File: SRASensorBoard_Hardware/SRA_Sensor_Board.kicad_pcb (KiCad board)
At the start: 2 copper layers, 70 parts, among them J1 USB_B_Micro, Q1 CSD17305Q5A, U1 LM3478MMX_NOPB, U2 OKI, U3 OKI, U4 TM4C129E_Launchpad, U5 MAX232, U6 IRF7821PbF

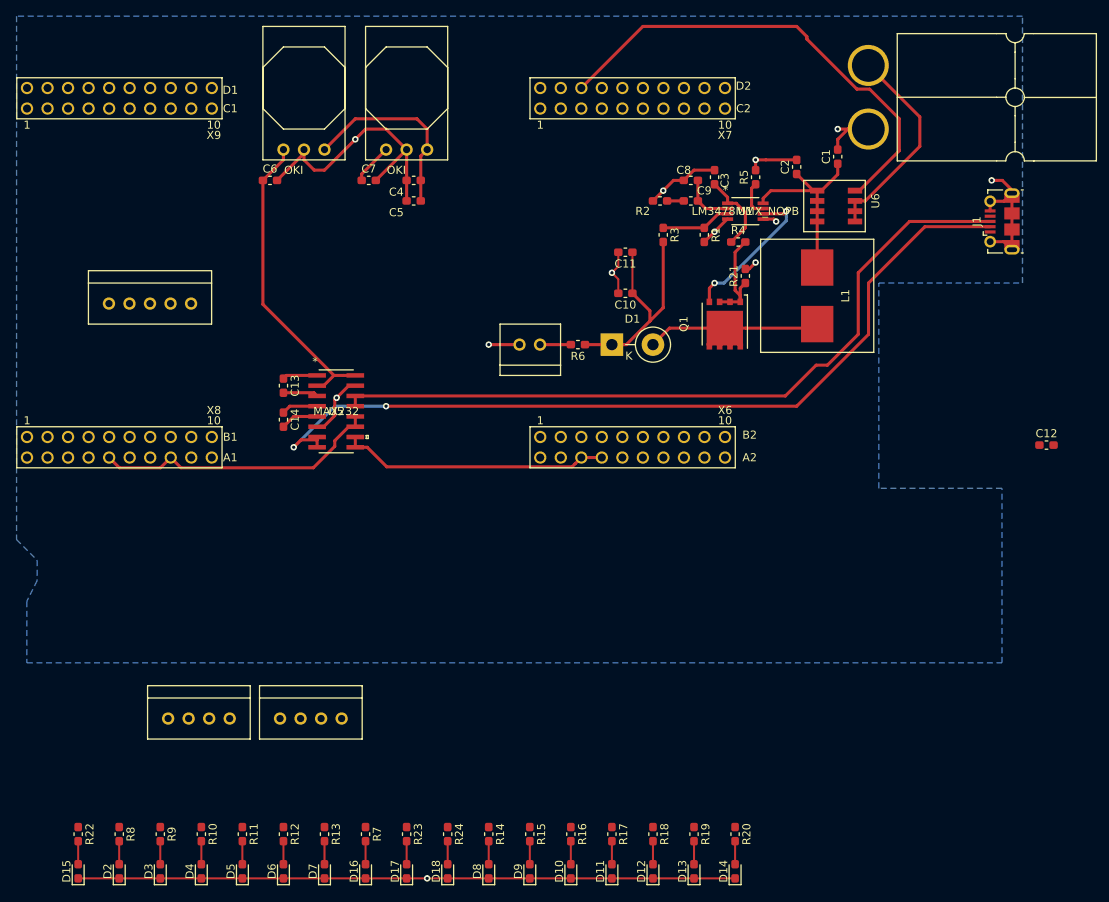
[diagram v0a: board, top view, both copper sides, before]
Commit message: Fixed some more routing
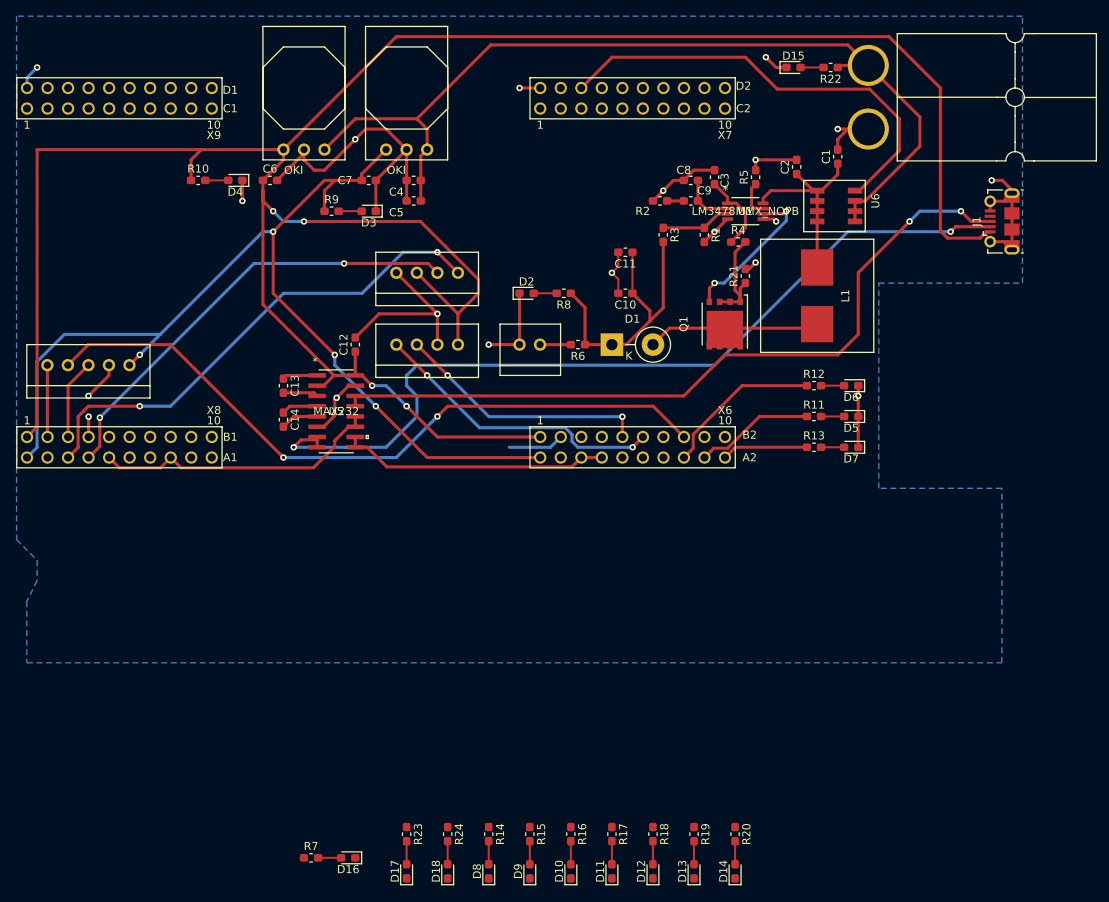
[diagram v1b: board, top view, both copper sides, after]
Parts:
- moved D15 133.1 mm to (158.4, 43.2), turned to 0 degrees
- moved R22 132.9 mm to (163.0, 43.2), turned to 180 degrees
- moved D5 94.0 mm to (165.5, 86.4), turned to 180 degrees
- moved D6 92.4 mm to (165.5, 82.5), turned to 180 degrees
- moved R11 87.6 mm to (160.9, 86.4), turned to 0 degrees
- moved D2 87.5 mm to (125.3, 71.1), turned to 0 degrees
- moved R8 86.6 mm to (129.9, 71.1), turned to 180 degrees
- moved C12 86.4 mm to (104.1, 77.5), turned to 90 degrees
- moved R12 86.0 mm to (160.9, 82.5), turned to 0 degrees
- moved D3 85.7 mm to (105.8, 61.0), turned to 180 degrees
- moved D4 85.6 mm to (89.3, 57.1), turned to 180 degrees
- moved D7 83.7 mm to (165.5, 90.2), turned to 180 degrees
- moved R10 80.9 mm to (84.7, 57.1), turned to 0 degrees
- moved R9 79.9 mm to (101.2, 61.0), turned to 0 degrees
- moved R13 77.2 mm to (160.9, 90.2), turned to 0 degrees
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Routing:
- net +5V: track 37.9 -> 300.2 mm, vias 0 -> 4
- net +3V3: track 5.06 -> 126.4 mm, vias 0 -> 4
- net CCD_OS: track 0.00 -> 87.3 mm, vias 0 -> 2
- net +12V: track 50.0 -> 114.7 mm
- net C02_In: track 0.00 -> 62.1 mm, vias 0 -> 2
- net C02_Out: track 0.00 -> 55.7 mm, vias 0 -> 2
- net Flow_Output: track 0.00 -> 36.8 mm, vias 0 -> 2
- net Flow_Receive: track 0.00 -> 31.6 mm, vias 0 -> 2
- net SW_Flag1: track 0.00 -> 19.9 mm
- net SW_Flag2: track 0.00 -> 14.8 mm
- net GND: track 181.0 -> 166.9 mm, vias 12 -> 17
- net SW_ERROR: track 0.00 -> 10.7 mm
- net CCD_INT1: track 0.00 -> 9.93 mm
- net CCD_INT2: track 0.00 -> 7.38 mm, vias 0 -> 2
- net +24V: track 29.1 -> 36.2 mm
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
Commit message: Changes to board
LED area is currently being made. Slight changes to wiring. Added schematic for SMD diode. Overall structure is the same.
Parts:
- removed U4: TM4C129E_Launchpad, MRDT_Shields:TM4C129E_Launchpad_FULL_THT_TOP
- D1: value 950mV 10A -> SBRD10200TR; footprint Diode_THT:D_5W_P5.08mm_Vertical_KathodeUp -> MRDT_ICs:SMC_DPAK
- moved D13 130.9 mm to (84.6, 27.1)
- moved R19 130.9 mm to (84.6, 22.5)
- moved D10 130.9 mm to (69.3, 27.1)
- moved D11 130.9 mm to (74.4, 27.1)
- moved D12 130.9 mm to (79.5, 27.1)
- moved D14 130.9 mm to (89.7, 27.1)
- moved D16 130.9 mm to (41.8, 25.4)
- moved D17 130.9 mm to (49.0, 27.1)
- moved D18 130.9 mm to (54.1, 27.1)
- moved D8 130.9 mm to (59.2, 27.1)
- moved D9 130.9 mm to (64.3, 27.1)
- moved R14 130.9 mm to (59.2, 22.5)
- moved R15 130.9 mm to (64.3, 22.5)
- moved R16 130.9 mm to (69.3, 22.5)
- moved R17 130.9 mm to (74.4, 22.5)
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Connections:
- D1 pad 1: +24V -> Net-(D1-Pad1)
- D1 pad 2: Net-(D1-Pad2) -> Net-(D1-Pad1)
- L1 pad 2: Net-(D1-Pad2) -> Net-(D1-Pad1)
- Q1 pad 5: Net-(D1-Pad2) -> Net-(D1-Pad1)
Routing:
- net +5V: track 300.2 -> 2.10 mm, vias 4 -> 0
- net GND: track 166.9 -> 106.6 mm, vias 17 -> 9
- net Net-(D1-Pad2): track 29.3 -> 0.00 mm
- net Net-(D1-Pad1): track 0.00 -> 27.7 mm
- net SW_Flag1: track 19.9 -> 0.00 mm
- net SW_Flag2: track 14.8 -> 0.00 mm
- net SW_ERROR: track 10.7 -> 0.00 mm
- net Flow_Output: track 36.8 -> 29.8 mm
- net C02_Out: track 55.7 -> 62.6 mm, vias 2 -> 1
- net Flow_Receive: track 31.6 -> 24.7 mm
- net C02_In: track 62.1 -> 66.7 mm, vias 2 -> 1
- net +12V: track 114.7 -> 111.1 mm
- net +3V3: track 126.4 -> 123.0 mm
- net +24V: track 36.2 -> 39.1 mm, vias 0 -> 1
- net Net-(Conn5-Pad1): track 3.81 -> 5.73 mm
- added copper zone on F.Cu, net +5V

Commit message: Board Update
Layout is done. All traces are done. LEDs are done.
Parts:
- added U4: TM4C129E_Launchpad, MRDT_Shields:TM4C129E_Launchpad_FULL_THT_TOP, F.Cu at (62.2, 93.7)
- moved R7 54.1 mm to (83.8, 52.8), turned to 180 degrees
- moved R17 49.2 mm to (84.2, 70.7), turned to 180 degrees
- moved R23 48.1 mm to (83.8, 55.7), turned to 180 degrees
- moved R16 47.7 mm to (84.2, 67.8), turned to 180 degrees
- moved R24 46.9 mm to (83.9, 58.6), turned to 180 degrees
- moved R15 46.7 mm to (84.1, 64.7), turned to 180 degrees
- moved R14 46.5 mm to (84.1, 61.7), turned to 180 degrees
- moved D16 46.3 mm to (79.2, 52.8), turned to 0 degrees
- moved C12 45.7 mm to (74.5, 42.7), turned to 0 degrees
- moved D11 44.0 mm to (79.6, 70.7), turned to 0 degrees
- moved R20 43.7 mm to (100.2, 64.9), turned to 180 degrees
- moved R19 42.2 mm to (99.9, 61.8), turned to 180 degrees
- moved D10 42.0 mm to (79.6, 67.8), turned to 0 degrees
- moved R18 41.6 mm to (99.9, 58.8), turned to 180 degrees
- moved D17 41.6 mm to (79.2, 55.7), turned to 0 degrees
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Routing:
- net SW_ERROR: track 0.00 -> 94.6 mm, vias 0 -> 4
- net SW_Flag2: track 0.00 -> 90.5 mm, vias 0 -> 1
- net SW_Flag1: track 0.00 -> 82.4 mm, vias 0 -> 1
- net +24V: track 39.1 -> 116.5 mm, vias 1 -> 2
- net LED_Enable: track 55.6 -> 125.6 mm, vias 0 -> 2
- net CCD_OS: track 87.3 -> 142.3 mm, vias 2 -> 10
- net Flow_Receive: track 24.7 -> 77.3 mm, vias 2 -> 4
- net CCD_INT2: track 7.38 -> 56.7 mm, vias 2 -> 3
- net Flow_Output: track 29.8 -> 78.4 mm, vias 2 -> 5
- net CCD_INT1: track 9.93 -> 53.5 mm, vias 0 -> 3
- net USB_TIVA_2: track 33.3 -> 74.1 mm, vias 0 -> 4
- net C02_Out: track 62.6 -> 97.3 mm, vias 1 -> 4
- net GND: track 106.6 -> 138.7 mm
- net +12V: track 111.1 -> 142.6 mm, vias 0 -> 1
- net USB_TIVA_1: track 35.8 -> 66.9 mm, vias 0 -> 2
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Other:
- board text added: "12V"
- board text added: "24V"
- board text added: "3.3V"
- board text added: "5V"
- board text added: "CCD"
- board text added: "CCDINT1"
- board text added: "CCDINT2"
- board text added: "CCD_OS"
- board text added: "CO2In"
- board text added: "CO2Out"
- board text added: "Error"
- board text added: "Flag1"
- board text added: "Flag2"
- board text added: "FlowOut"
- board text added: "FlowRec"
- board text added: "LED"
- board text added: "Power"
- board text added: "SW"
- board text added: "Sensors"
- board text added: "USB1"
- board text added: "USB2"

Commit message: Forgot a ground connection
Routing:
- net GND: track 138.7 -> 146.7 mm, vias 9 -> 10
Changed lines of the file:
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@@
     (thickness 1.6)
     (drawings 54)
-    (tracks 651)
+    (tracks 657)
     (zones 0)
     (modules 70)
@@
   (segment (start 184.4755 64.73) (end 184.6255 64.88) (width 0.25) (layer F.Cu) (net 1))
   (segment (start 181.9255 64.73) (end 184.4755 64.73) (width 0.25) (layer F.Cu) (net 1))
+  (segment (start 77.5716 40.8178) (end 75.41 40.8178) (width 0.25) (layer F.Cu) (net 1))
+  (segment (start 78.9686 40.8178) (end 78.9686 40.8178) (width 0.25) (layer F.Cu) (net 1))
+  (segment (start 75.3732 42.6974) (end 77.089 42.6974) (width 0.25) (layer F.Cu) (net 1))
+  (segment (start 77.089 42.6974) (end 78.9686 40.8178) (width 0.25) (layer F.Cu) (net 1))
+  (segment (start 78.9686 40.8178) (end 77.5716 40.8178) (width 0.25) (layer F.Cu) (net 1))
+  (via (at 78.9686 40.8178) (size 0.8) (drill 0.4) (layers F.Cu B.Cu) (net 1))
   (segment (start 161.29 62.23) (end 161.29 60.96) (width 0.381) (layer F.Cu) (net 2))
   (segment (start 161.29 60.96) (end 161.29 59.69) (width 0.381) (layer F.Cu) (net 2))

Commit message: Cleaned Some Things
Signatures and shem visual changes
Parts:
- added G***: LOGO, footprints:Toni_Signature_Rev4, F.Cu at (171.4, 110.5)
- added G***: , custom:Don_Signature_Medium, F.Cu at (171.4, 108.0)
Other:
- board text added: "SRA Sensors Board, Rev 1 Mars Rover, 20XX Missouri S&T Donald Shaw, Toni Ramljak Andy Yang, Jacob VanDoren"

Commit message: Added Step Files
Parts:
- added G***: LOGO, MRDT_Silkscreens:0_MRDT_Logo_7.5mm, F.Cu at (161.3, 102.1)
-  : renamed from G***; value LOGO -> (none)
-  : renamed from G***
- moved J1 0.54 mm to (183.9, 62.2)
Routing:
- net USB_Data_2: track 102.7 -> 103.3 mm
- net USB_Data_1: track 93.5 -> 94.1 mm
- net GND: vias 10 -> 11
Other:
- board outline added: 124.5 x 81.3 mm

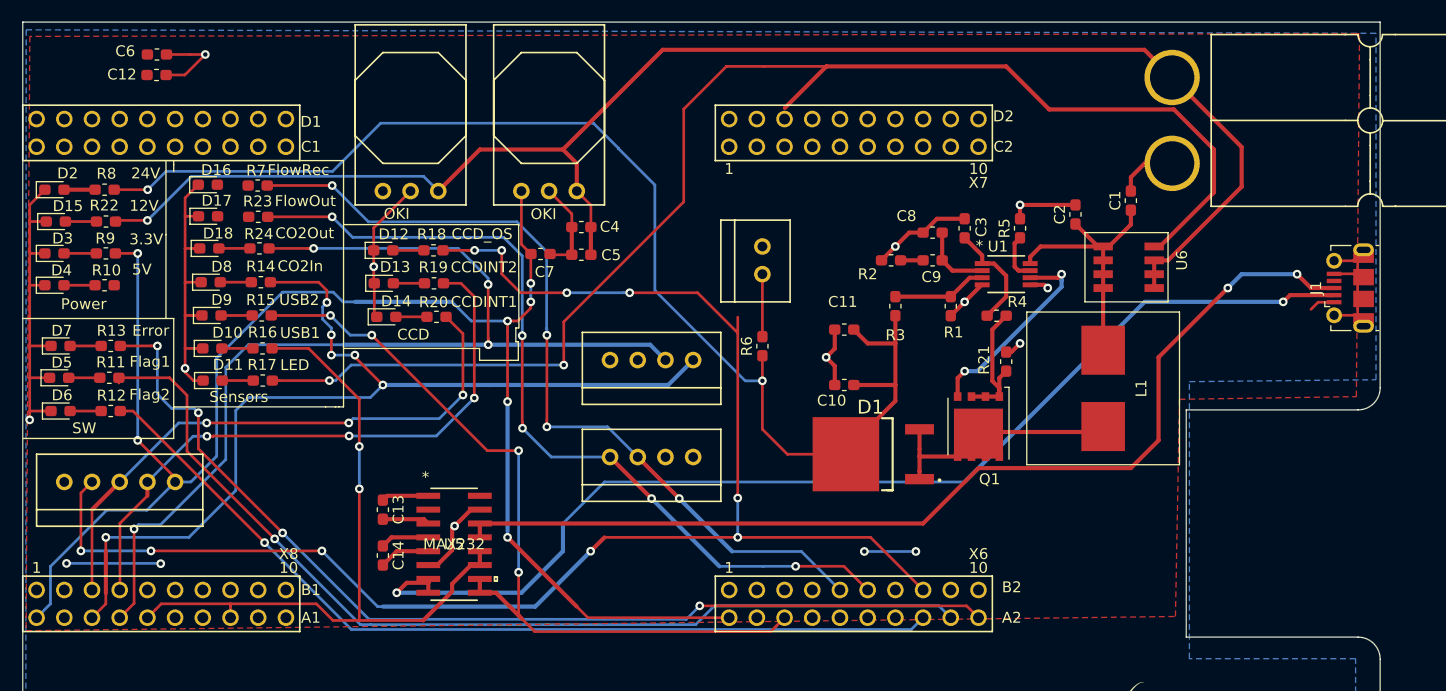
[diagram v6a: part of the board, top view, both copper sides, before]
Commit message: Updates
Updated traces on board

Changed resistor values to be in compliance with best practices

Regenerated STEP and GERBER files for updated board

Added TIVA and Connections text files
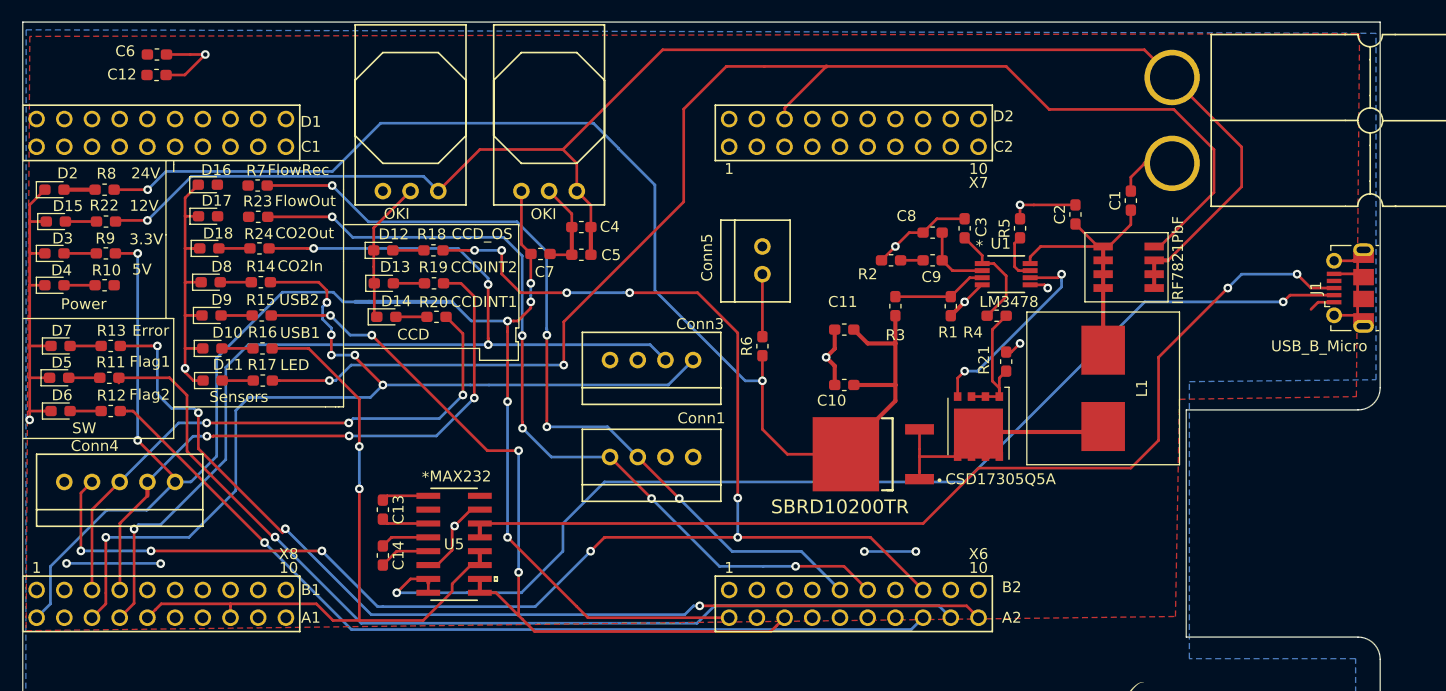
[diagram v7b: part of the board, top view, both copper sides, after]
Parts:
- R10, R11, R12, R13, R14, R15, R16, R17, R18, R19, R20, R23, R24, R7: value 500 -> 510
- R9: value 500 -> 330
- U1: value LM3478MMX_NOPB -> LM3478
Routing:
- net CCD_OS: track 142.3 -> 140.9 mm
- net LED_Enable: track 125.6 -> 126.6 mm
- net GND: vias 11 -> 10

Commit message: Updates
Added footprints. Created new board. Something is up with the andersons.
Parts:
- removed  : , footprints:Toni_Signature_Rev4
- removed  : , custom:Don_Signature_Medium
- removed C10, C11: 82uF, Capacitor_SMD:C_0603_1608Metric_Pad1.05x0.95mm_HandSolder
- removed C12, C13, C14: 1uF, Capacitor_SMD:C_0603_1608Metric_Pad1.05x0.95mm_HandSolder
- removed C3: 10pF, Capacitor_SMD:C_0603_1608Metric_Pad1.05x0.95mm_HandSolder
- removed C8: 1nF, Capacitor_SMD:C_0603_1608Metric_Pad1.05x0.95mm_HandSolder
- removed C9: 22nF, Capacitor_SMD:C_0603_1608Metric_Pad1.05x0.95mm_HandSolder
- removed D1: SBRD10200TR, MRDT_ICs:SMC_DPAK
- removed G***: LOGO, MRDT_Silkscreens:0_MRDT_Logo_7.5mm
- removed L1: 4.7uH 11.2mOhm, custom:Donald_Shaw_SRP1270
- added Conn10: UV_LED_V+_2, MRDT_Connectors:Anderson_2_Horizontal_Stacked, F.Cu at (301.0, 104.9)
- added Conn11: UV_LED_GND, MRDT_Connectors:Anderson_2_Horizontal_Stacked, F.Cu at (168.1, 156.5)
- added Conn6: 24v Boost, MRDT_Connectors:Anderson_2_Horizontal_Side_by_Side, F.Cu at (255.8, 99.8)
- added Conn7: Boost GND, MRDT_Connectors:Anderson_2_Horizontal_Stacked, F.Cu at (273.1, 118.9)
- added Conn8: Boost GND, MRDT_Connectors:Anderson_2_Horizontal_Stacked, F.Cu at (167.9, 167.1)
- added Conn9: UV_LED_V+_1, MRDT_Connectors:Anderson_2_Horizontal_Stacked, F.Cu at (235.5, 128.5)
- added Q2: BSS138, Package_TO_SOT_SMD:SOT-23, F.Cu at (242.1, 47.7)
- added Q3: BSS138, Package_TO_SOT_SMD:SOT-23, F.Cu at (242.1, 43.2)
- added Q4: BSS138, Package_TO_SOT_SMD:SOT-23, F.Cu at (191.0, 111.7)
- added R25: 10K, Resistor_SMD:R_0603_1608Metric_Pad1.05x0.95mm_HandSolder, F.Cu at (190.9, 115.3)
- added R26: 10K, Resistor_SMD:R_0603_1608Metric_Pad1.05x0.95mm_HandSolder, F.Cu at (199.7, 110.7)
- added R27: 10K, Resistor_SMD:R_0603_1608Metric_Pad1.05x0.95mm_HandSolder, F.Cu at (190.9, 117.8)
- C1: value 120uF -> 0.1 uF
- C2: value 100nF -> .1 uF
- Conn5: value Molex_SL_02 -> 12v Boost; footprint MRDT_Connectors:MOLEX_SL_02_Vertical -> MRDT_Connectors:Anderson_2_Horizontal_Side_by_Side
- J1: value USB_B_Micro -> USB_A; footprint Connector_USB:USB_Micro-B_Molex-105017-0001 -> Connector_USB:USB3_A_Molex_48393-001
- Q1: value CSD17305Q5A -> BSS138; footprint Package_TO_SOT_SMD:TDSON-8-1 -> Package_TO_SOT_SMD:SOT-23
- R1: value 18.2k -> 10K
- R2: value 3.48k -> 10K
- R21: value 6m -> 10K
- R3: value 18.2k -> 4
- R4: value 100 -> 4
- R5: value 26.7k -> 10K
- R6: value 3.33 -> 10K
- U1: value LM3478 -> LT1910; footprint custom:LM3478MMX&slash_NOPB -> MRDT_ICs:SOIC127P599X175-8N
- U4: footprint MRDT_Shields:TM4C129E_Launchpad_FULL_THT_TOP -> MRDT_Shields:TM4C129E_Launchpad_FULL_THT_BOTTOM
- U5: value MAX232 -> IRF7821PbF; footprint footprints:MAX232DR -> MRDT_ICs:IRF7821PBF
- U6: value IRF7821PbF -> FT232RL; footprint footprints:IRF7821PBF -> Package_SO:SSOP-28_5.3x10.2mm_P0.65mm
- moved R8 165.1 mm to (234.2, 67.7), turned to 0 degrees
- moved R10 164.9 mm to (234.2, 72.8), turned to 0 degrees
- moved R9 164.8 mm to (234.2, 70.2), turned to 0 degrees
- moved C6 155.3 mm to (222.8, 87.1)
- moved Conn5 152.3 mm to (281.9, 72.1), turned to 0 degrees
- moved R17 150.1 mm to (234.2, 75.3), turned to 0 degrees
- moved R22 147.2 mm to (211.3, 96.9), turned to 0 degrees
- moved R11 143.2 mm to (211.3, 94.4), turned to 0 degrees
- moved R13 140.3 mm to (207.0, 99.4), turned to 0 degrees
- moved R19 138.9 mm to (238.6, 70.2), turned to 0 degrees
- moved R12 138.7 mm to (207.0, 96.9), turned to 0 degrees
- moved U2 129.4 mm to (229.2, 41.7), turned to 0 degrees
- moved Conn2 126.4 mm to (230.9, 160.3), turned to 0 degrees
- moved R7 125.7 mm to (195.4, 110.7), turned to 0 degrees
- moved R16 125.6 mm to (207.0, 94.4), turned to 0 degrees
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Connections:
- C2 pad 1: Net-(C1-Pad1) -> Reset
- C2 pad 2: GND -> Net-(C2-Pad2)
- Conn1 pad 3: Flow_Receive -> O2_TX
- Conn1 pad 4: Flow_Output -> O2_RX
- Conn3 pad 1: C02_In -> +5V
- Conn3 pad 2: C02_Out -> GND
- Conn3 pad 3: +5V -> C02_TX
- Conn3 pad 4: GND -> C02_RX
- Conn4 pad 2: CCD_INT2 -> GND
- Conn4 pad 3: CCD_INT1 -> CCD_INT2
- Conn4 pad 4: CCD_OS -> CCD_INT1
- Conn4 pad 5: GND -> CCD_OS
- Conn5 pad 1: Net-(Conn5-Pad1) -> (no net)
- Conn5 pad 2: GND -> +12V
- J1 pad 2: USB_Data_2 -> USB_Data-
- J1 pad 3: USB_Data_1 -> USB_Data+
- J1 pad 4: Net-(J1-Pad4) -> GND
- J1 pad 6: GND -> (no net)
- Q1 pad 1: Net-(Q1-Pad1) -> +3V3
- Q1 pad 2: Net-(Q1-Pad1) -> TIVA_O2_TX
- Q1 pad 3: Net-(Q1-Pad1) -> O2_RX
- R1 pad 1: Net-(R1-Pad1) -> +3V3
- R1 pad 2: GND -> TIVA_O2_TX
- R14 pad 1: C02_In -> C02_RX
- R15 pad 1: USB_TIVA_2 -> TIVA_USB_RX
- R16 pad 1: USB_TIVA_1 -> TIVA_USB_TX
- R2 pad 1: Net-(C9-Pad2) -> +3V3
- R2 pad 2: GND -> TIVA_CO2_TX
- R21 pad 1: Net-(Q1-Pad1) -> +3V3
- R21 pad 2: GND -> TIVA_O2_RX
- R23 pad 1: Flow_Output -> O2_TX
- R24 pad 1: C02_Out -> C02_TX
- R3 pad 1: Net-(R1-Pad1) -> Net-(R3-Pad1)
- R3 pad 2: +24V -> Net-(Conn9-Pad2)
- R4 pad 1: Net-(C3-Pad1) -> Net-(R3-Pad1)
- R4 pad 2: Net-(Q1-Pad1) -> Net-(Conn10-Pad2)
- R5 pad 1: Net-(R5-Pad1) -> +5V
- R5 pad 2: GND -> O2_RX
- R6 pad 1: +24V -> +5V
- R6 pad 2: Net-(Conn5-Pad1) -> C02_RX
- R7 pad 1: Flow_Receive -> O2_RX
- U1 pad 1: Net-(C3-Pad1) -> GND
- U1 pad 3: Net-(R1-Pad1) -> Net-(U1-Pad3)
- U1 pad 4: GND -> LED_Enable
- U1 pad 5: GND -> Net-(U1-Pad5)
- U1 pad 6: Net-(Q1-Pad4) -> +12V
- U1 pad 7: Net-(R5-Pad1) -> (no net)
- U1 pad 8: Net-(C1-Pad1) -> +12V
- U4 pad PC6: USB_TIVA_1 -> TIVA_USB_RX
- U4 pad PC7: USB_TIVA_1 -> TIVA_USB_TX
- U4 pad PP0: USB_TIVA_2 -> Net-(U4-PadPP0)
- U4 pad PP1: USB_TIVA_2 -> Net-(U4-PadPP1)
- U5 pad 1: Net-(C13-Pad1) -> Net-(R3-Pad1)
- U5 pad 2: +5V -> Net-(R3-Pad1)
- U5 pad 3: Net-(C13-Pad2) -> Net-(R3-Pad1)
- U5 pad 4: Net-(C14-Pad1) -> Net-(U1-Pad5)
- U5 pad 5: Net-(C14-Pad2) -> +12V
- U5 pad 6: GND -> +12V
- U5 pad 7: USB_Data_2 -> +12V
- U5 pad 8: USB_Data_2 -> +12V
- U6 pad 1: +12V -> TIVA_USB_RX
- U6 pad 2: +12V -> Net-(C2-Pad2)
- U6 pad 3: +12V -> Net-(U6-Pad3)
- U6 pad 4: LED_Enable -> +3V3
- U6 pad 5: Net-(C1-Pad1) -> TIVA_USB_TX
- U6 pad 6: Net-(C1-Pad1) -> Net-(U6-Pad6)
- U6 pad 7: Net-(C1-Pad1) -> GND
- U6 pad 8: Net-(C1-Pad1) -> (no net)
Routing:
- net GND: track 146.7 -> 0.00 mm, vias 10 -> 0
- net +3V3: track 145.4 -> 0.00 mm, vias 7 -> 0
- net +12V: track 142.6 -> 0.00 mm, vias 1 -> 0
- net CCD_OS: track 140.9 -> 0.00 mm, vias 10 -> 0
- net LED_Enable: track 126.6 -> 0.00 mm, vias 2 -> 0
- net +24V: track 116.5 -> 0.00 mm, vias 2 -> 0
- net USB_Data_2: track 103.4 -> 0.00 mm, vias 2 -> 0
- net C02_Out: track 97.3 -> 0.00 mm, vias 4 -> 0
- net SW_ERROR: track 94.1 -> 0.00 mm, vias 4 -> 0
- net USB_Data_1: track 94.1 -> 0.00 mm, vias 2 -> 0
- net C02_In: track 90.6 -> 0.00 mm, vias 6 -> 0
- net SW_Flag2: track 90.5 -> 0.00 mm, vias 1 -> 0
- net SW_Flag1: track 82.4 -> 0.00 mm, vias 1 -> 0
- net Flow_Output: track 78.4 -> 0.00 mm, vias 5 -> 0
- net Flow_Receive: track 77.3 -> 0.00 mm, vias 4 -> 0
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- removed copper zone on F.Cu, net +5V
- removed copper zone on B.Cu, net GND
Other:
- board outline removed
- board text removed: "12V"
- board text removed: "24V"
- board text removed: "3.3V"
- board text removed: "5V"
- board text removed: "CCD"
- board text removed: "CCDINT1"
- board text removed: "CCDINT2"
- board text removed: "CCD_OS"
- board text removed: "CO2In"
- board text removed: "CO2Out"
- board text removed: "Error"
- board text removed: "Flag1"
- board text removed: "Flag2"
- board text removed: "FlowOut"
- board text removed: "FlowRec"
- board text removed: "LED"
- board text removed: "Power"
- board text removed: "SRA Sensors Board, Rev 1 Mars Rover, 20XX Missouri S&T Donald Shaw, Toni Ramljak Andy Yang, Jacob VanDoren"
- board text removed: "SW"
- board text removed: "Sensors"
- board text removed: "USB1"
- board text removed: "USB2"
